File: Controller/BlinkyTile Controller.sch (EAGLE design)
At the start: 27 parts, among them CON1 USB_MICROSMT+THRUHULE, CON2 F-2X05-DIL-100, Q1 CRYSTAL_4PAD2520, SW1 SPST_TACT-EVQQ2, SW2 SPST_TACT-EVQQ2, U1 MK20D--VFM5, U2 W25Q80BV, U3 74LVC1G17DCK, U4 74LVC1G17DCK, U5 74LVC1G17DCK

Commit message: Controller: Change .1" header footprint to Sparkfun version, make text larger
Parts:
- removed CON2: F-2X05-DIL-100, con-headers-jp:F-2X05-DIL-100
- removed TP1: ADCIN, solpad:SE11
- added JP1: M05X2NO_SILK, SparkFun-Connectors:M05X2NO_SILK
- added JP3: M01PTH, SparkFun-Connectors:M01PTH
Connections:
- net +3V3: now also JP1.1; no longer CON2.1
- net ADC15: now also JP3.1; no longer TP1.MP
- net GND: now also JP1.2; no longer CON2.2
- net PA4: now also JP1.7; no longer CON2.7
- net PB0: now also JP1.9; no longer CON2.9
- net PB1: now also JP1.10; no longer CON2.10
- net RESET: now also JP1.8; no longer CON2.8
- net RX: now also JP1.4; no longer CON2.4
- net TCLK: now also JP1.3; no longer CON2.3
- net TMS: now also JP1.6; no longer CON2.6
- net TX: now also JP1.5; no longer CON2.5
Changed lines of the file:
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@@
 <part name="GND5" library="supply1" deviceset="GND" device=""/>
 <part name="TP2" library="solpad" deviceset="SE11" device="" value="ADDRESS"/>
-<part name="TP1" library="solpad" deviceset="SE11" device="" value="ADCIN"/>
-<part name="CON2" library="con-headers-jp" deviceset="F-2X05-" device="DIL-100" value="F-2X05-DIL-100"/>
 <part name="U3" library="74xx-little-us" deviceset="74*1G17" device="DCK" technology="LVC"/>
 <part name="T1" library="zetex" deviceset="PMOSSOT23" device=""/>
@@
 <part name="GND11" library="supply1" deviceset="GND" device=""/>
 <part name="3V4" library="supply1" deviceset="+3V3" device=""/>
+<part name="JP1" library="SparkFun-Connectors" deviceset="M05X2" device="NO_SILK"/>
+<part name="JP3" library="SparkFun-Connectors" deviceset="M01" device="PTH"/>
 </parts>
 <sheets>
@@
 <instance part="GND5" gate="1" x="269.24" y="119.38"/>
 <instance part="TP2" gate="1" x="307.34" y="91.44" rot="MR0"/>
-<instance part="TP1" gate="1" x="175.26" y="190.5" rot="MR90"/>
-<instance part="CON2" gate="G$1" x="45.72" y="132.08"/>
 <instance part="U3" gate="G$1" x="337.82" y="124.46" smashed="yes">
 <attribute name="NAME" x="339.09" y="127.635" size="1.778" layer="95"/>
@@
 <attribute name="VALUE" x="320.04" y="146.05" size="1.778" layer="96"/>
 </instance>
+<instance part="JP1" gate="G$1" x="45.72" y="132.08"/>
+<instance part="JP3" gate="G$1" x="180.34" y="190.5" rot="R180"/>
 </instances>
 <busses>
@@
 </segment>
 <segment>
-<pinref part="CON2" gate="G$1" pin="2"/>
 <wire x1="53.34" y1="137.16" x2="60.96" y2="137.16" width="0.1524" layer="91"/>
 <label x="55.88" y="137.16" size="1.778" layer="95"/>
+<pinref part="JP1" gate="G$1" pin="2"/>
 </segment>
 <segment>
@@
 </segment>
 <segment>
-<pinref part="CON2" gate="G$1" pin="1"/>
 <wire x1="38.1" y1="137.16" x2="27.94" y2="137.16" width="0.1524" layer="91"/>
 <label x="27.94" y="137.16" size="1.778" layer="95"/>
+<pinref part="JP1" gate="G$1" pin="1"/>
 </segment>
 <segment>
@@
 <net name="TCLK" class="0">
 <segment>
-<pinref part="CON2" gate="G$1" pin="3"/>
 <wire x1="38.1" y1="134.62" x2="27.94" y2="134.62" width="0.1524" layer="91"/>
 <label x="27.94" y="134.62" size="1.778" layer="95"/>
+<pinref part="JP1" gate="G$1" pin="3"/>
 </segment>
 <segment>
@@
 </segment>
 <segment>
-<pinref part="CON2" gate="G$1" pin="6"/>
 <wire x1="53.34" y1="132.08" x2="60.96" y2="132.08" width="0.1524" layer="91"/>
 <label x="55.88" y="132.08" size="1.778" layer="95"/>
+<pinref part="JP1" gate="G$1" pin="6"/>
 </segment>
 </net>
@@
 </segment>
 <segment>
-<pinref part="CON2" gate="G$1" pin="4"/>
 <wire x1="60.96" y1="134.62" x2="53.34" y2="134.62" width="0.1524" layer="91"/>
 <label x="55.88" y="134.62" size="1.778" layer="95"/>
+<pinref part="JP1" gate="G$1" pin="4"/>
 </segment>
 </net>
@@
 </segment>
 <segment>
-<pinref part="CON2" gate="G$1" pin="5"/>
 <wire x1="38.1" y1="132.08" x2="27.94" y2="132.08" width="0.1524" layer="91"/>
 <label x="27.94" y="132.08" size="1.778" layer="95"/>
+<pinref part="JP1" gate="G$1" pin="5"/>
 </segment>
 </net>
@@
 </segment>
 <segment>
-<pinref part="CON2" gate="G$1" pin="8"/>
 <wire x1="53.34" y1="129.54" x2="60.96" y2="129.54" width="0.1524" layer="91"/>
 <label x="55.88" y="129.54" size="1.778" layer="95"/>
+<pinref part="JP1" gate="G$1" pin="8"/>
 </segment>
 </net>
@@
 <wire x1="147.32" y1="190.5" x2="172.72" y2="190.5" width="0.1524" layer="91"/>
 <label x="154.94" y="190.5" size="1.778" layer="95"/>
-<pinref part="TP1" gate="1" pin="MP"/>
+<pinref part="JP3" gate="G$1" pin="1"/>
 </segment>
 </net>
@@
 </segment>
 <segment>
-<pinref part="CON2" gate="G$1" pin="7"/>
 <wire x1="38.1" y1="129.54" x2="27.94" y2="129.54" width="0.1524" layer="91"/>
 <label x="27.94" y="129.54" size="1.778" layer="95"/>
+<pinref part="JP1" gate="G$1" pin="7"/>
 </segment>
 </net>
@@
 </segment>
 <segment>
-<pinref part="CON2" gate="G$1" pin="9"/>
 <wire x1="38.1" y1="127" x2="27.94" y2="127" width="0.1524" layer="91"/>
 <label x="27.94" y="127" size="1.778" layer="95"/>
+<pinref part="JP1" gate="G$1" pin="9"/>
 </segment>
 </net>
@@
 </segment>
 <segment>
-<pinref part="CON2" gate="G$1" pin="10"/>
 <wire x1="53.34" y1="127" x2="60.96" y2="127" width="0.1524" layer="91"/>
 <label x="55.88" y="127" size="1.778" layer="95"/>
-</segment>
-</net>
+<pinref part="JP1" gate="G$1" pin="10"/>
+</segment>
+</net>

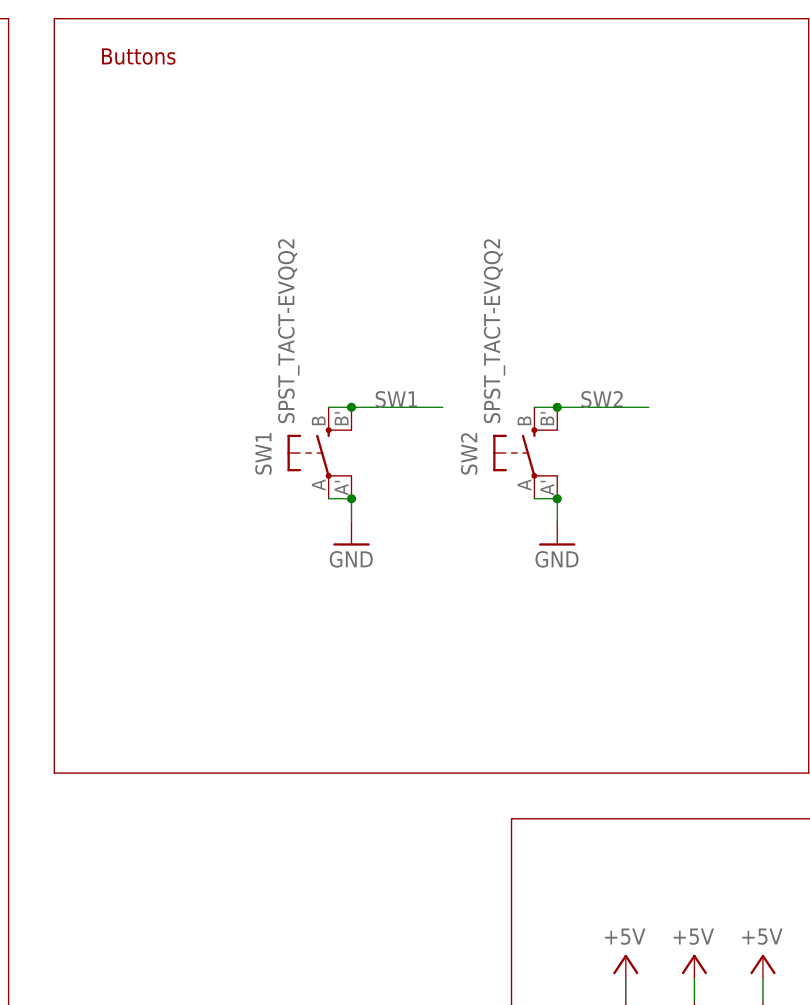
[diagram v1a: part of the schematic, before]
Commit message: Controller: move end of 3.3v trace to improve grounding, replace switch, resize 5v line
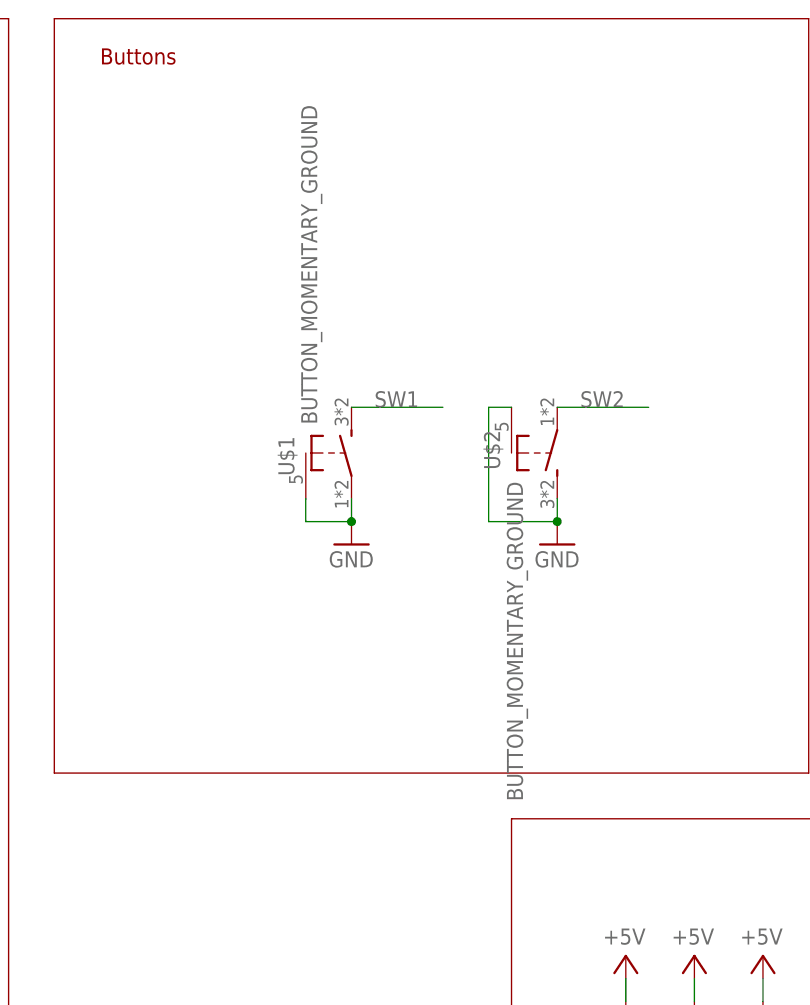
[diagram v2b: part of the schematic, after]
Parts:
- removed SW1, SW2: SPST_TACT-EVQQ2, adafruit:SPST_TACT-EVQQ2
- added U$1, U$2: BUTTON_MOMENTARY_GROUND, blinkinlabs:BUTTON_MOMENTARY_GROUND
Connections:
- net GND: now also U$1.P, U$1.SHIELD, U$2.S, U$2.SHIELD; no longer SW1.P, SW1.P1, SW2.P, SW2.P1
- net SW1: now also U$1.S; no longer SW1.S, SW1.S1
- net SW2: now also U$2.P; no longer SW2.S, SW2.S1
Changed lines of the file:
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@@
 <part name="R4" library="adafruit" deviceset="R-US_" device="R0402" value="330"/>
 <part name="LED1" library="adafruit" deviceset="LED" device="CHIPLED_0805" value="STATUS"/>
-<part name="SW1" library="adafruit" deviceset="SPST_TACT" device="-EVQQ2"/>
 <part name="GND12" library="supply1" deviceset="GND" device=""/>
 <part name="3V3" library="supply1" deviceset="+3V3" device=""/>
@@
 <part name="3V2" library="supply1" deviceset="+3V3" device=""/>
 <part name="L1" library="rcl" deviceset="L-EU" device="L1812" value="1812L260THDR"/>
-<part name="SW2" library="adafruit" deviceset="SPST_TACT" device="-EVQQ2"/>
 <part name="GND2" library="supply1" deviceset="GND" device=""/>
 <part name="U4" library="74xx-little-us" deviceset="74*1G17" device="DCK" technology="LVC"/>
@@
 <part name="JP1" library="SparkFun-Connectors" deviceset="M05X2" device="NO_SILK"/>
 <part name="JP3" library="SparkFun-Connectors" deviceset="M01" device="PTH"/>
+<part name="U$1" library="blinkinlabs" deviceset="BUTTON_MOMENTARY_GROUND" device=""/>
+<part name="U$2" library="blinkinlabs" deviceset="BUTTON_MOMENTARY_GROUND" device=""/>
 </parts>
 <sheets>
@@
 <instance part="R4" gate="G$1" x="187.96" y="185.42" rot="R90"/>
 <instance part="LED1" gate="G$1" x="187.96" y="175.26"/>
-<instance part="SW1" gate="G$1" x="236.22" y="200.66"/>
 <instance part="GND12" gate="1" x="238.76" y="190.5"/>
 <instance part="3V3" gate="G$1" x="187.96" y="195.58" smashed="yes">
@@
 </instance>
 <instance part="L1" gate="G$1" x="53.34" y="195.58" rot="R90"/>
-<instance part="SW2" gate="G$1" x="259.08" y="200.66"/>
 <instance part="GND2" gate="1" x="261.62" y="190.5"/>
 <instance part="U4" gate="G$1" x="337.82" y="104.14" smashed="yes">
@@
 <instance part="JP1" gate="G$1" x="45.72" y="132.08"/>
 <instance part="JP3" gate="G$1" x="180.34" y="190.5" rot="R180"/>
+<instance part="U$1" gate="G$1" x="236.22" y="200.66"/>
+<instance part="U$2" gate="G$1" x="259.08" y="200.66" rot="MR180"/>
 </instances>
 <busses>
@@
 </segment>
 <segment>
-<pinref part="SW1" gate="G$1" pin="P"/>
-<pinref part="SW1" gate="G$1" pin="P1"/>
-<wire x1="236.22" y1="195.58" x2="238.76" y2="195.58" width="0.1524" layer="91"/>
-<pinref part="GND12" gate="1" pin="GND"/>
-<wire x1="238.76" y1="195.58" x2="238.76" y2="193.04" width="0.1524" layer="91"/>
-<junction x="238.76" y="195.58"/>
-</segment>
-<segment>
 <pinref part="C3" gate="G$1" pin="2"/>
 <pinref part="GND19" gate="1" pin="GND"/>
 <wire x1="71.12" y1="205.74" x2="71.12" y2="208.28" width="0.1524" layer="91"/>
-</segment>
-<segment>
-<pinref part="SW2" gate="G$1" pin="P"/>
-<pinref part="SW2" gate="G$1" pin="P1"/>
-<wire x1="259.08" y1="195.58" x2="261.62" y2="195.58" width="0.1524" layer="91"/>
-<pinref part="GND2" gate="1" pin="GND"/>
-<wire x1="261.62" y1="195.58" x2="261.62" y2="193.04" width="0.1524" layer="91"/>
-<junction x="261.62" y="195.58"/>
 </segment>
 <segment>
@@
 <pinref part="GND11" gate="1" pin="GND"/>
 <wire x1="78.74" y1="208.28" x2="78.74" y2="205.74" width="0.1524" layer="91"/>
+</segment>
+<segment>
+<pinref part="GND2" gate="1" pin="GND"/>
+<pinref part="U$2" gate="G$1" pin="S"/>
+<wire x1="261.62" y1="195.58" x2="261.62" y2="193.04" width="0.1524" layer="91"/>
+<pinref part="U$2" gate="G$1" pin="SHIELD"/>
+<wire x1="256.54" y1="205.74" x2="254" y2="205.74" width="0.1524" layer="91"/>
+<wire x1="254" y1="205.74" x2="254" y2="193.04" width="0.1524" layer="91"/>
+<wire x1="254" y1="193.04" x2="261.62" y2="193.04" width="0.1524" layer="91"/>
+<junction x="261.62" y="193.04"/>
+</segment>
+<segment>
+<pinref part="U$1" gate="G$1" pin="P"/>
+<pinref part="GND12" gate="1" pin="GND"/>
+<wire x1="238.76" y1="195.58" x2="238.76" y2="193.04" width="0.1524" layer="91"/>
+<wire x1="238.76" y1="193.04" x2="233.68" y2="193.04" width="0.1524" layer="91"/>
+<pinref part="U$1" gate="G$1" pin="SHIELD"/>
+<wire x1="233.68" y1="193.04" x2="233.68" y2="195.58" width="0.1524" layer="91"/>
+<junction x="238.76" y="193.04"/>
 </segment>
 </net>
@@
 <net name="SW1" class="0">
 <segment>
-<pinref part="SW1" gate="G$1" pin="S1"/>
-<pinref part="SW1" gate="G$1" pin="S"/>
-<wire x1="238.76" y1="205.74" x2="236.22" y2="205.74" width="0.1524" layer="91"/>
-<junction x="238.76" y="205.74"/>
 <wire x1="238.76" y1="205.74" x2="248.92" y2="205.74" width="0.1524" layer="91"/>
 <label x="241.3" y="205.74" size="1.778" layer="95"/>
+<pinref part="U$1" gate="G$1" pin="S"/>
 </segment>
 <segment>
@@
 <net name="SW2" class="0">
 <segment>
-<pinref part="SW2" gate="G$1" pin="S1"/>
-<pinref part="SW2" gate="G$1" pin="S"/>
-<wire x1="261.62" y1="205.74" x2="259.08" y2="205.74" width="0.1524" layer="91"/>
-<junction x="261.62" y="205.74"/>
+<label x="264.16" y="205.74" size="1.778" layer="95"/>
+<pinref part="U$2" gate="G$1" pin="P"/>
 <wire x1="261.62" y1="205.74" x2="271.78" y2="205.74" width="0.1524" layer="91"/>
-<label x="264.16" y="205.74" size="1.778" layer="95"/>
-</segment>
-<segment>
+</segment>
+<segment>

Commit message: Change 4p output connector, push switches in a bit
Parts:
- removed TP2: ADDRESS, solpad:SE11
- SV1: device dodocohedreled:4-PIN_DUPONT -> blinkinlabs:4-PIN_DUPONT
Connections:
- net N$4: no longer TP2.MP
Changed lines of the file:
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@@
 <layer number="56" name="wert" color="7" fill="1" visible="no" active="no"/>
 <layer number="57" name="tCAD" color="7" fill="1" visible="no" active="no"/>
+<layer number="90" name="Modules" color="5" fill="1" visible="yes" active="yes"/>
 <layer number="91" name="Nets" color="2" fill="1" visible="yes" active="yes"/>
 <layer number="92" name="Busses" color="1" fill="1" visible="yes" active="yes"/>
@@
 <part name="P+3" library="supply1" deviceset="+5V" device=""/>
 <part name="GND5" library="supply1" deviceset="GND" device=""/>
-<part name="TP2" library="solpad" deviceset="SE11" device="" value="ADDRESS"/>
 <part name="U3" library="74xx-little-us" deviceset="74*1G17" device="DCK" technology="LVC"/>
 <part name="T1" library="zetex" deviceset="PMOSSOT23" device=""/>
@@
 <part name="C6" library="adafruit" deviceset="C-US" device="C0402" value="100nF"/>
 <part name="R5" library="adafruit" deviceset="R-US_" device="R0402" value="10k"/>
-<part name="SV1" library="dodocohedreled" deviceset="4-PIN_DUPONT" device=""/>
+<part name="SV1" library="blinkinlabs" deviceset="4-PIN_DUPONT" device=""/>
 <part name="C8" library="adafruit" deviceset="C-US" device="C0805K" value="10uF"/>
 <part name="GND11" library="supply1" deviceset="GND" device=""/>
@@
 </instance>
 <instance part="GND5" gate="1" x="269.24" y="119.38"/>
-<instance part="TP2" gate="1" x="307.34" y="91.44" rot="MR0"/>
 <instance part="U3" gate="G$1" x="337.82" y="124.46" smashed="yes">
 <attribute name="NAME" x="339.09" y="127.635" size="1.778" layer="95"/>
@@
 <segment>
 <pinref part="U5" gate="G$1" pin="O"/>
-<pinref part="TP2" gate="1" pin="MP"/>
-<wire x1="307.34" y1="88.9" x2="297.18" y2="88.9" width="0.1524" layer="91"/>
 <pinref part="SV1" gate="1" pin="3"/>
 <wire x1="365.76" y1="101.6" x2="345.44" y2="101.6" width="0.1524" layer="91"/>
 <wire x1="345.44" y1="101.6" x2="345.44" y2="88.9" width="0.1524" layer="91"/>
-<wire x1="345.44" y1="88.9" x2="307.34" y2="88.9" width="0.1524" layer="91"/>
-<junction x="307.34" y="88.9"/>
-</segment>
-</net>
+<wire x1="345.44" y1="88.9" x2="297.18" y2="88.9" width="0.1524" layer="91"/>
+</segment>
+</net>
